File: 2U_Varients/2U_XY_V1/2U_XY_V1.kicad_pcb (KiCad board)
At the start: 4 copper layers, 83 x 213 mm, 35 parts, among them CN1 DF11-2DSA-4DP, J2 Conn_01x01, J3 Conn_01x01, J4 Conn_01x01, J5 Conn_01x01, U2 TMP112xxDRL, U3 DRV2605LDGS, U4 TCA4311ADGKR, U5 5040500691, U6 5040500691, U7 VEML6031X00

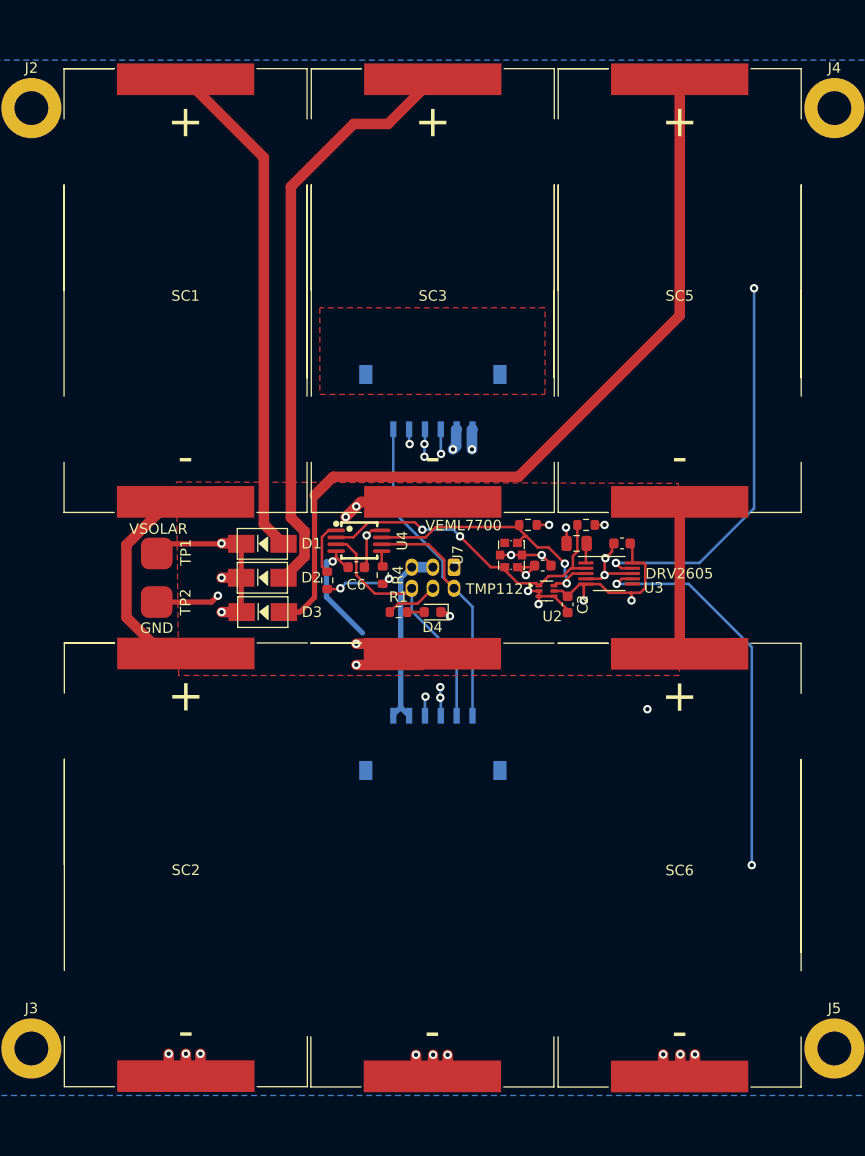
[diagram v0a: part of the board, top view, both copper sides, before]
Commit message: Created SM531K10T Libraries
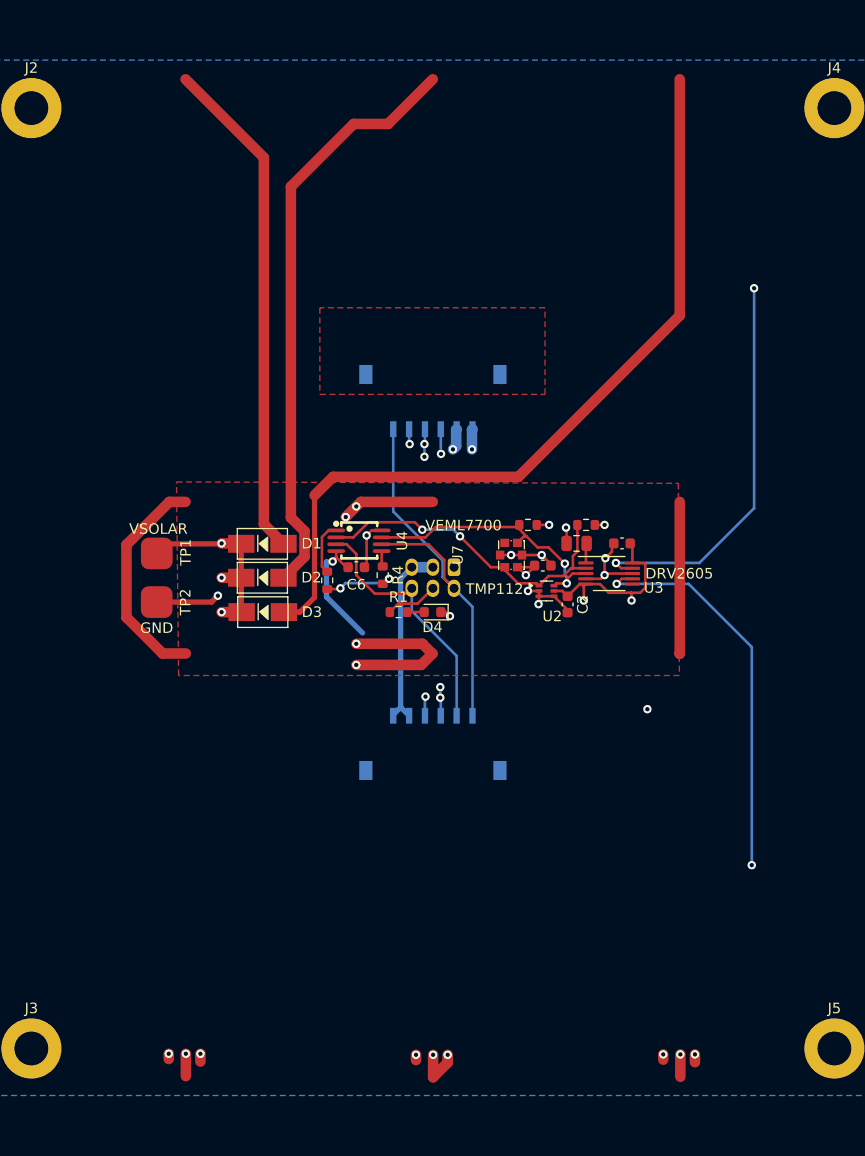
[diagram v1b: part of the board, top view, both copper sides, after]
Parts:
- removed SC1, SC2, SC3, SC4, SC5, SC6: SM101K07TF, SolarPanelBoards:KXOB101K08F-TR

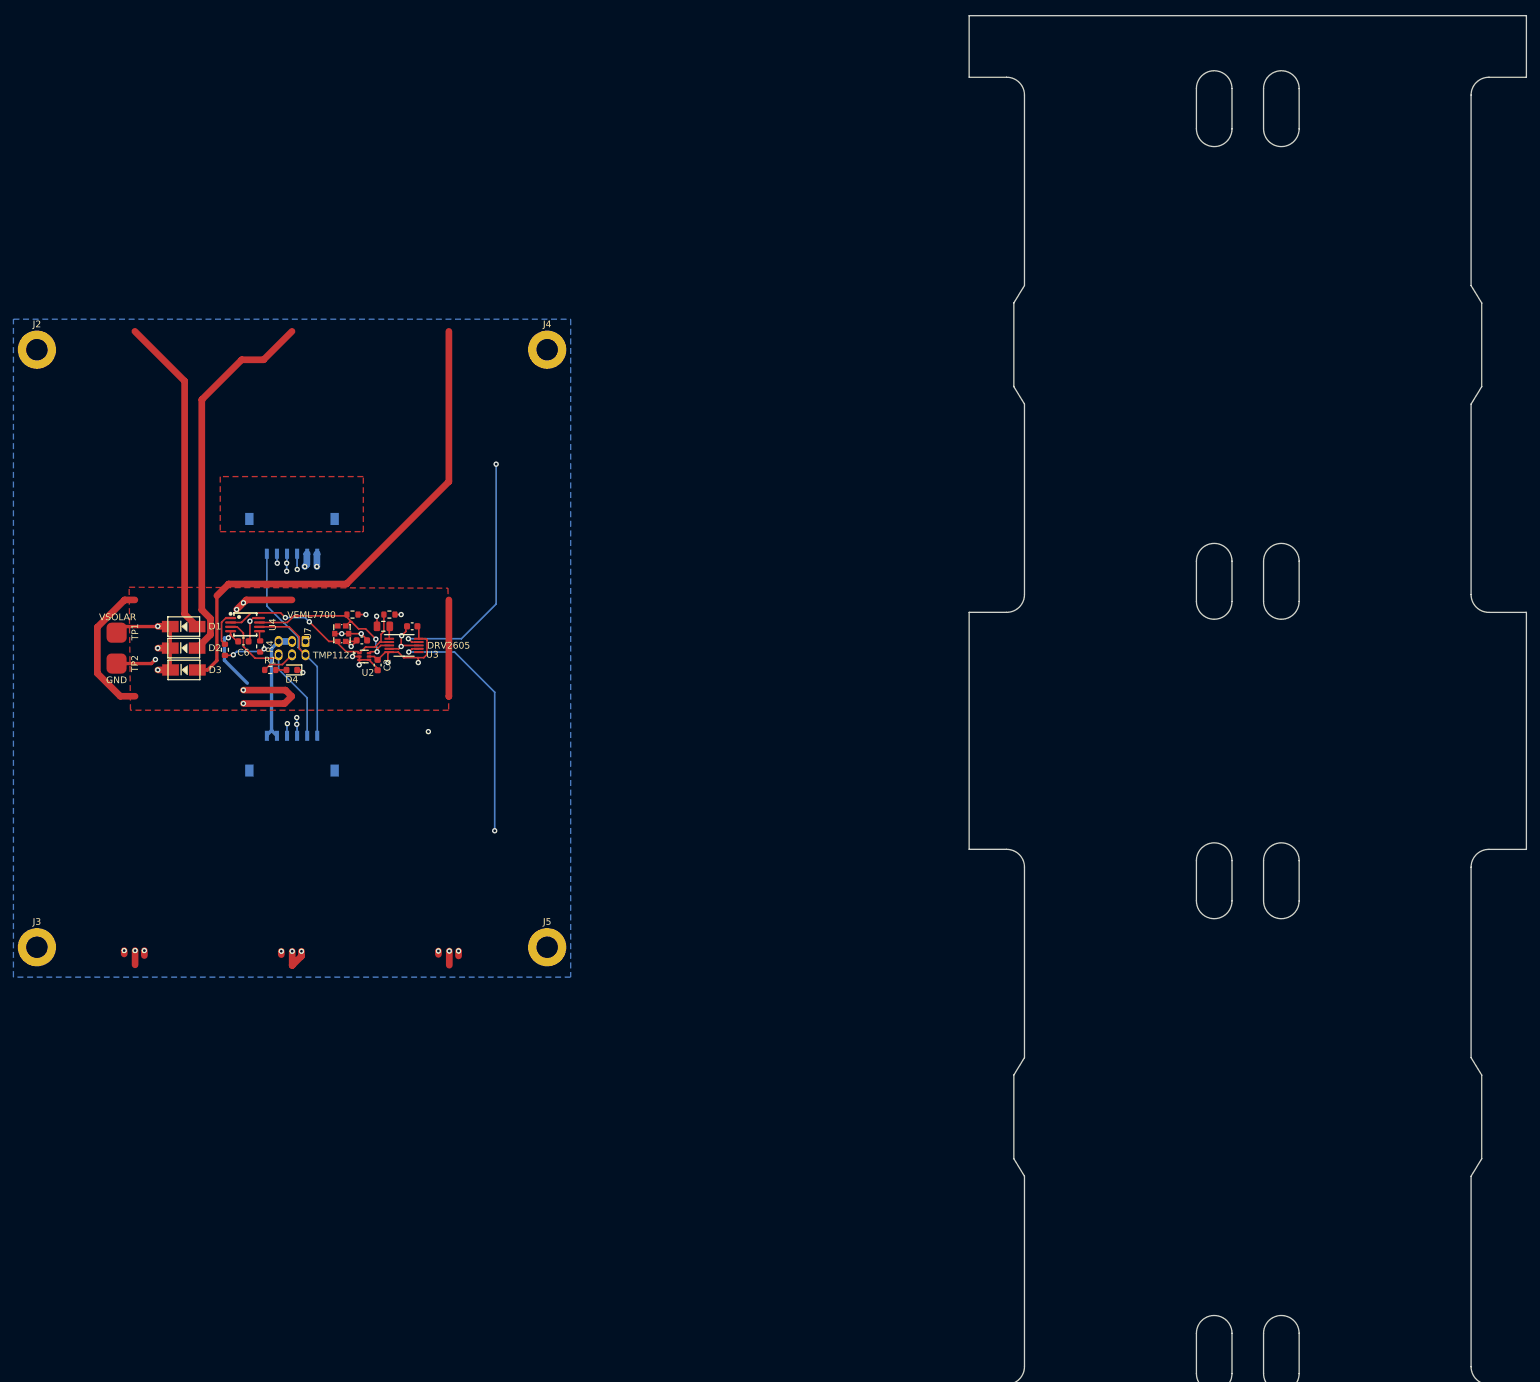
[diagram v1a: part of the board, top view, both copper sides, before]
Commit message: Added 3D Models to SM53
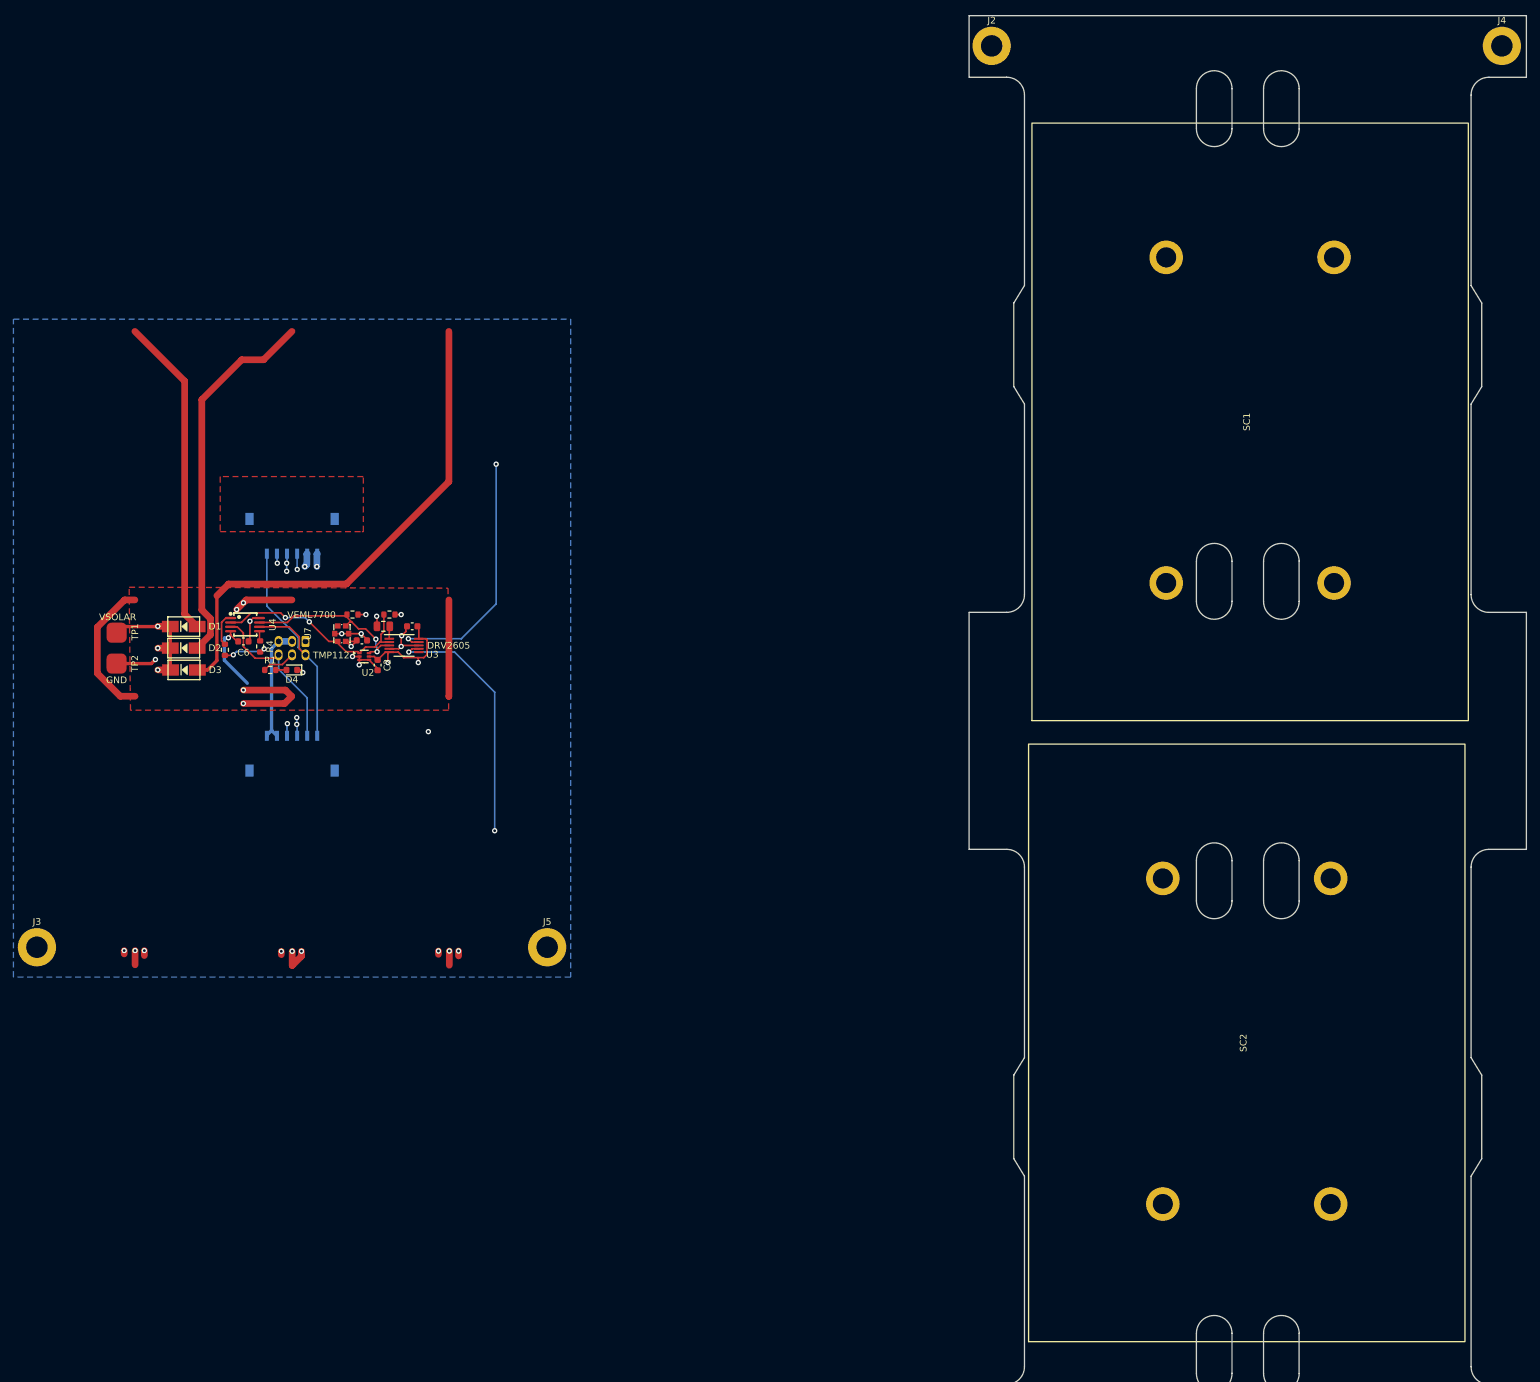
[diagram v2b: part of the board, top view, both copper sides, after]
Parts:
- added SC1: SM531K10T, Solar_Cell_Library:SM531K10T, F.Cu at (222.5, 72.0)
- added SC2: SM531K10T, Solar_Cell_Library:SM531K10T, F.Cu at (222.0, 164.5)
- moved J2 149.2 mm to (171.5, 40.5)
- moved J4 149.2 mm to (247.5, 40.5)
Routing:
- net (no net): track 0.00 -> 75.4 mm, vias 0 -> 4
- net Net-(SC3--): track 39.9 -> 0.00 mm, vias 4 -> 0
- net Net-(SC1--): track 21.2 -> 0.00 mm
- net Net-(SC5--): track 14.4 -> 0.00 mm
